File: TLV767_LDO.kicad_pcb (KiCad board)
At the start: 2 copper layers, 28.4 x 12.2 mm, 9 parts, among them J1 Conn_01x02_Pin, J2 Conn_01x02_Pin, U1 TLV76701DRVx

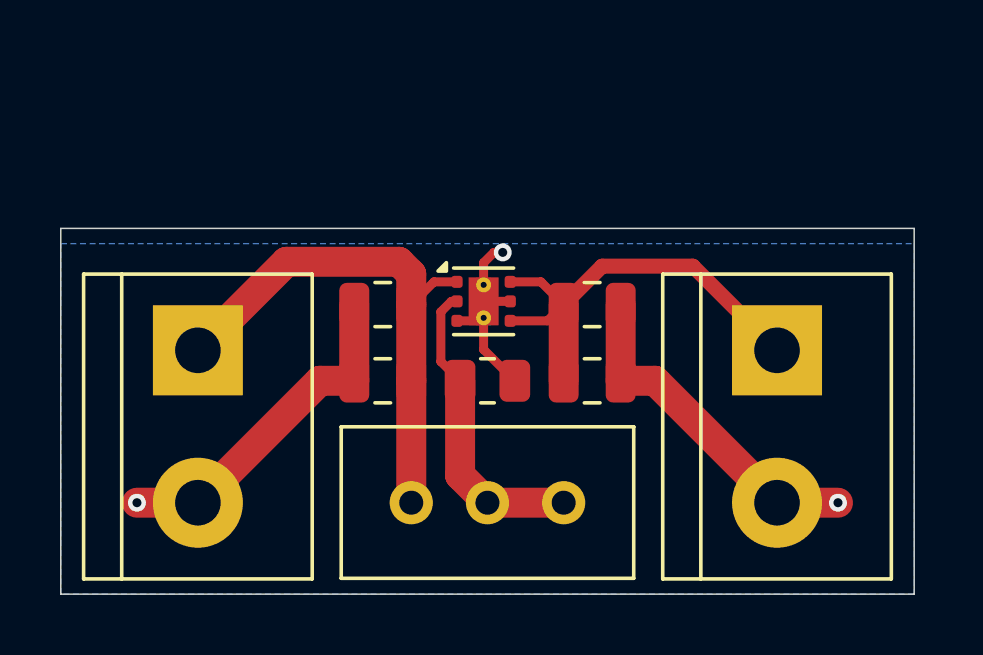
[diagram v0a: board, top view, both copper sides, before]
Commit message: Update 5V-to-3.3V design and add ERC/DRC reports
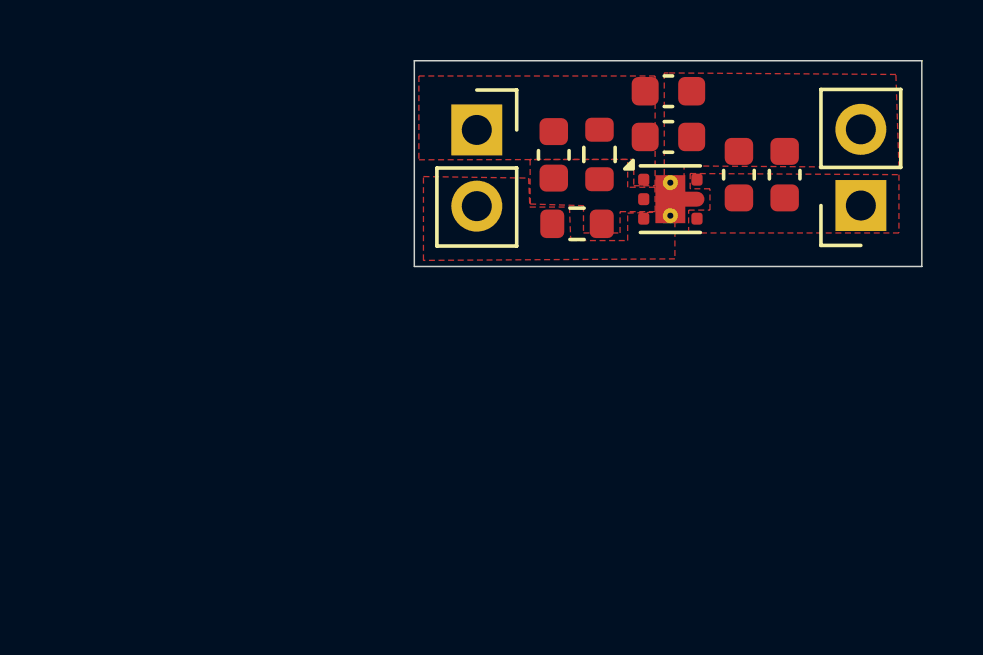
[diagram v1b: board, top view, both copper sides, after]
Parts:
- removed RV1: 500k, Potentiometer_THT:Potentiometer_Bourns_3296W_Vertical
- added C5: 10pF, Capacitor_SMD:C_0603_1608Metric, F.Cu at (157.7, 93.6)
- added R2: 32K, Resistor_SMD:R_0603_1608Metric, F.Cu at (158.4, 95.9)
- C1, C2, C4: footprint Capacitor_SMD:C_0805_2012Metric -> Capacitor_SMD:C_0603_1608Metric
- C3: value 1 uF -> 2.2uF; footprint Capacitor_SMD:C_0805_2012Metric -> Capacitor_SMD:C_0603_1608Metric
- J1, J2: footprint TerminalBlock:TerminalBlock_bornier-2_P5.08mm -> Connector_PinSocket_2.54mm:PinSocket_1x02_P2.54mm_Vertical
- R1: footprint Resistor_SMD:R_0805_2012Metric -> Resistor_SMD:R_0603_1608Metric
- moved C4 12.5 mm to (161.5, 93.0), turned to 0 degrees
- moved C3 11.9 mm to (161.5, 91.4), turned to 0 degrees
- moved J2 11.8 mm to (155.1, 92.7), turned to 0 degrees
- moved C2 8.43 mm to (163.8, 94.2), turned to 90 degrees
- moved R1 8.42 mm to (159.2, 93.5), turned to -90 degrees
- moved C1 7.74 mm to (165.4, 94.2), turned to 90 degrees
- moved U1 7.10 mm to (161.5, 95.0)
- moved J1 5.58 mm to (167.9, 95.2), turned to 180 degrees
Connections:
- net Net-(J1-Pin_1) renamed +5V
- C3 pad 1: Net-(J2-Pin_1) -> +3.3V
- C4 pad 1: Net-(J2-Pin_1) -> +3.3V
- J2 pad 1: Net-(J2-Pin_1) -> +3.3V
- R1 pad 1: Net-(U1-FB) -> +3.3V
- R1 pad 2: GND -> Net-(U1-FB)
- U1 pad 1: Net-(J2-Pin_1) -> +3.3V
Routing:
- net GND: track 29.9 -> 0.89 mm, vias 3 -> 0
- net Net-(J2-Pin_1): track 18.0 -> 0.00 mm
- net +5V: track 15.4 -> 0.00 mm
- net Net-(U1-FB): track 10.2 -> 0.00 mm
- added copper zone on F.Cu, net +3.3V
- added copper zone on F.Cu, net +5V
- added copper zone on F.Cu, net GND
- added copper zone on F.Cu, net Net-(U1-FB)
- removed copper zone on B.Cu, net GND
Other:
- board size 28.4 x 12.2 mm -> 16.9 x 6.9 mm
